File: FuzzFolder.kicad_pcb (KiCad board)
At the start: 4 copper layers, 50 x 60 mm, 61 parts, among them J101 PWR, J102 ScopeGroundLoop, Q101 BC857, Q102 BC847, Q103 BC857, Q104 BC847, U101 TL074, U102 LM741

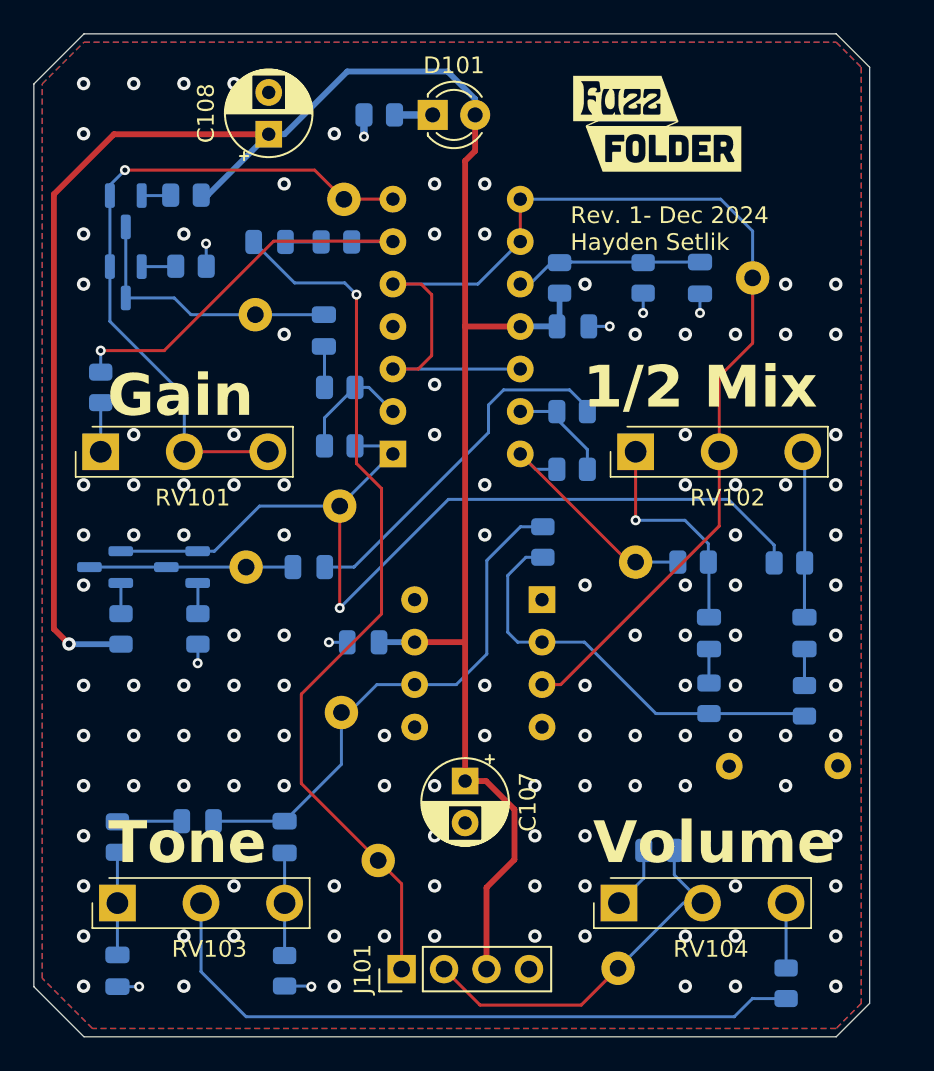
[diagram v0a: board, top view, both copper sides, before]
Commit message: 4layer sent to fab
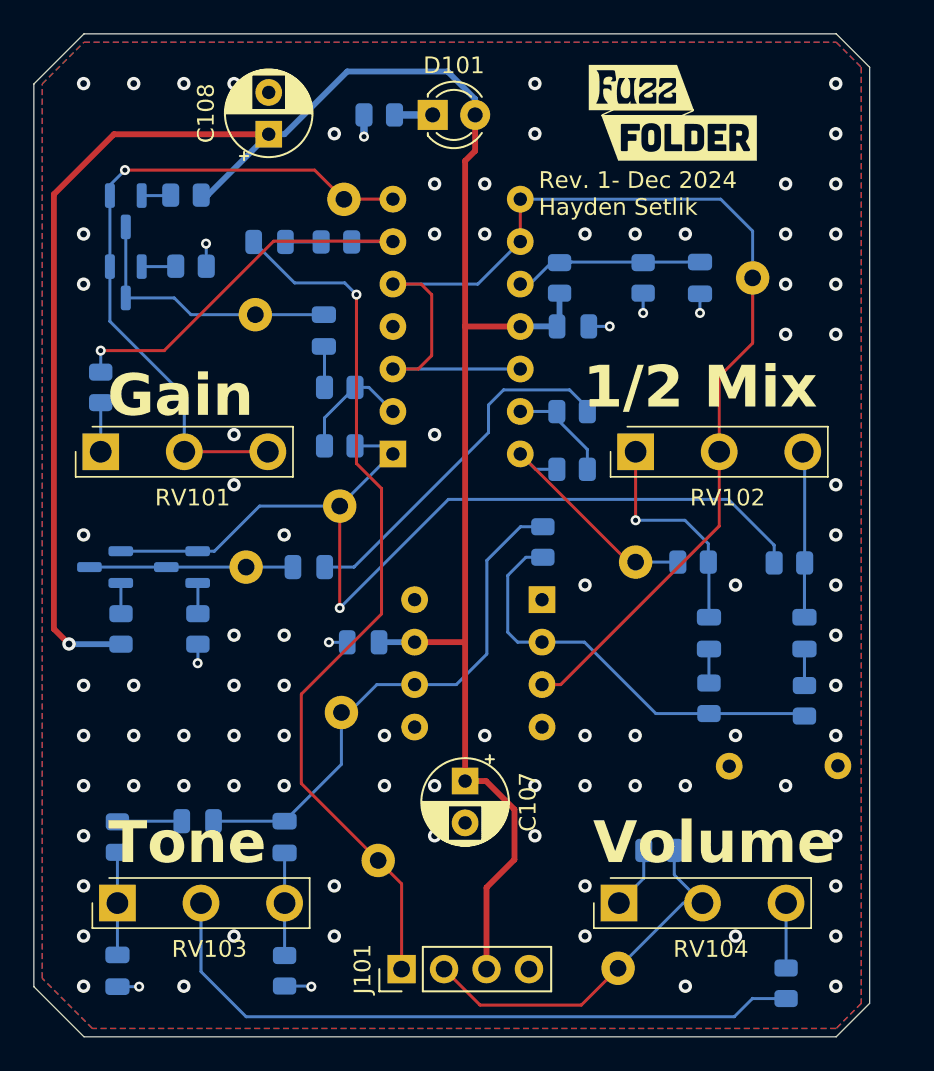
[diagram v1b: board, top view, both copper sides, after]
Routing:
- net GND: vias 131 -> 94
